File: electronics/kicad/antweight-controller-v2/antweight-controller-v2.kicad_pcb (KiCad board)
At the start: 2 copper layers, 30.5 x 58.4 mm, 11 parts, among them J10 3V3 GND VBAT_SW, J4 BATTERY, J5 MOTOR LEFT, J6 MOTOR RIGHT, J8 ESP32 LEFT ALL PINS, J9 ESP32 RIGHT SIGNALS, SW1 MAIN POWER, U1 ESP32-C3 SUPERMINI, U2 DRV8833, U3 3V3 BUCK-BOOST

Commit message: feat(electronics): finalize v2 controller layout
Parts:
- moved U2 14.7 mm to (22.0, 27.7), turned to 270 degrees
- moved C1_C2 5.08 mm to (18.0, 46.6)
- moved J10 5.08 mm to (12.7, 57.1)
- moved J4 5.08 mm to (18.0, 51.6)
- moved J5 5.08 mm to (4.50, 57.1)
- moved J6 5.08 mm to (25.9, 57.1)
- moved SW1 5.08 mm to (10.2, 51.6)
- moved U3 5.08 mm to (10.2, 46.6)
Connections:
- J9 pad 1: GPIO5_SPARE -> GPIO21_SPARE
- J9 pad 2: AIN2_GPIO6 -> GPIO20_SPARE
- J9 pad 3: AIN1_GPIO7 -> BIN2_GPIO10
- J9 pad 4: GPIO8_LED_EXPANSION -> BIN1_GPIO9
- J9 pad 5: BIN1_GPIO9 -> GPIO8_LED_EXPANSION
- J9 pad 6: BIN2_GPIO10 -> AIN1_GPIO7
- J9 pad 7: GPIO20_SPARE -> AIN2_GPIO6
- J9 pad 8: GPIO21_SPARE -> GPIO5_SPARE
- U1 pad 10: AIN2_GPIO6 -> GPIO20_SPARE
- U1 pad 11: AIN1_GPIO7 -> BIN2_GPIO10
- U1 pad 12: GPIO8_LED_EXPANSION -> BIN1_GPIO9
- U1 pad 13: BIN1_GPIO9 -> GPIO8_LED_EXPANSION
- U1 pad 14: BIN2_GPIO10 -> AIN1_GPIO7
- U1 pad 15: GPIO20_SPARE -> AIN2_GPIO6
- U1 pad 16: GPIO21_SPARE -> GPIO5_SPARE
- U1 pad 9: GPIO5_SPARE -> GPIO21_SPARE
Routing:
- net VBAT_RAW: track 0.00 -> 12.8 mm
- net GPIO4_SPARE: track 0.00 -> 2.54 mm
- net GPIO3_SPARE: track 0.00 -> 2.54 mm
- net GPIO2_SPARE: track 0.00 -> 2.54 mm
- net GPIO1_SPARE: track 0.00 -> 2.54 mm
- net GPIO0_SPARE: track 0.00 -> 2.54 mm
- net GND: track 0.00 -> 2.54 mm
- net 5V_NC: track 0.00 -> 2.54 mm
- net 3V3: track 0.00 -> 2.54 mm
- net GPIO8_LED_EXPANSION: track 0.00 -> 2.54 mm
- net GPIO5_SPARE: track 0.00 -> 2.54 mm
- net GPIO21_SPARE: track 0.00 -> 2.54 mm
- net GPIO20_SPARE: track 0.00 -> 2.54 mm
- net BIN2_GPIO10: track 0.00 -> 2.54 mm
- net BIN1_GPIO9: track 0.00 -> 2.54 mm
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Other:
- board size 30.5 x 58.4 mm -> 30.5 x 63.5 mm
- board text removed: "IN"

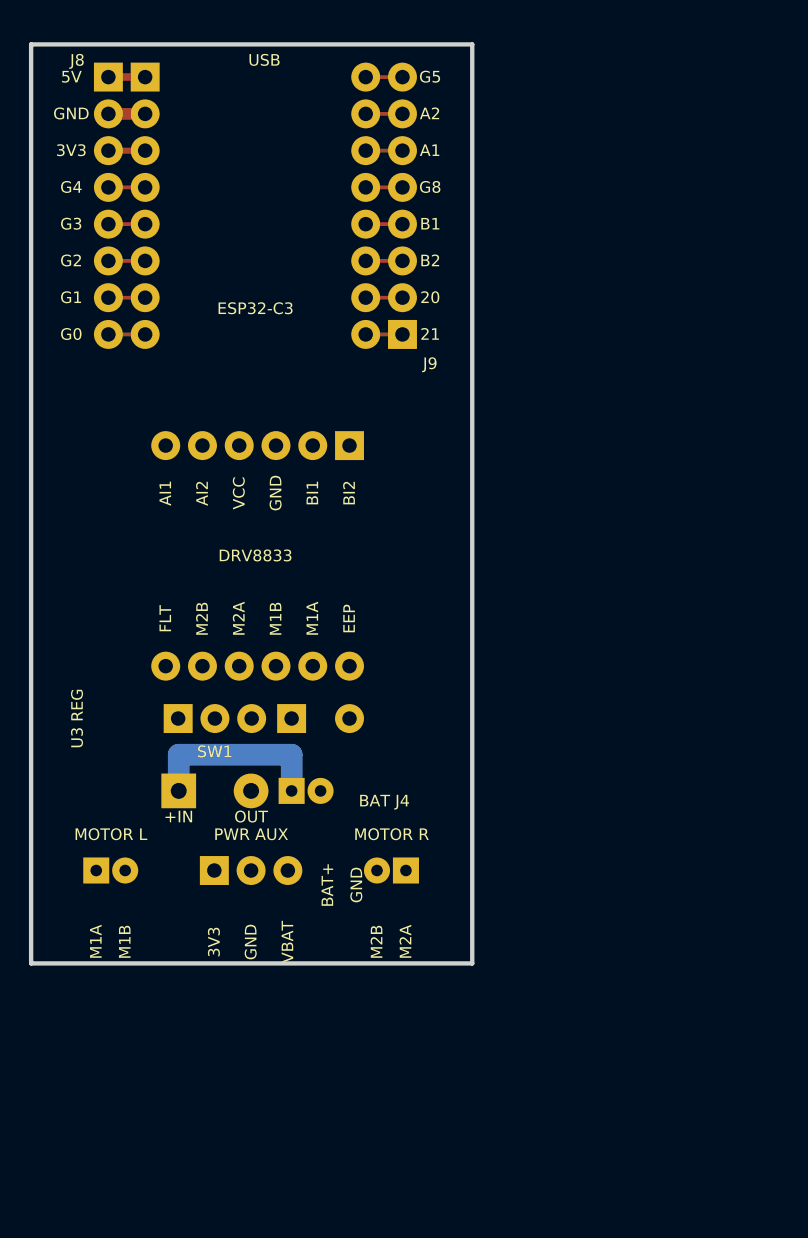
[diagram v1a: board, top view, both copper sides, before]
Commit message: Add 2S antweight controller design
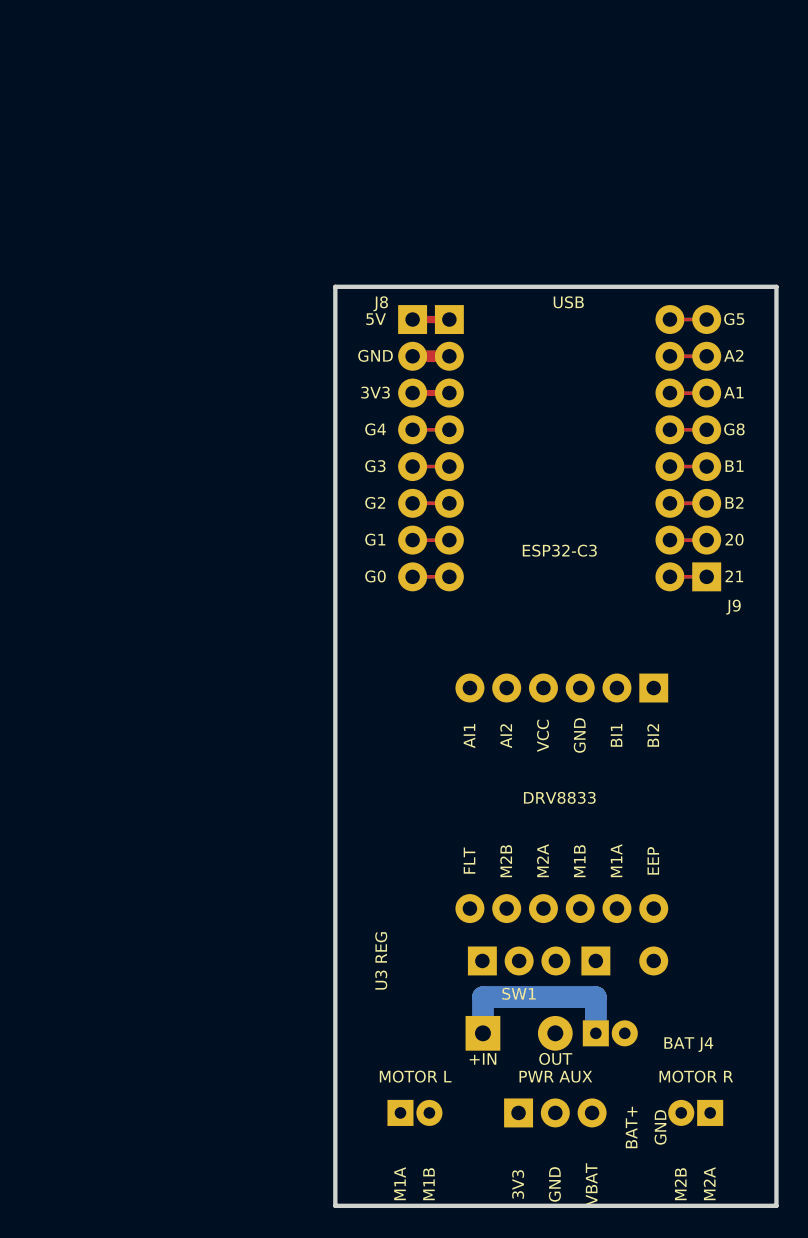
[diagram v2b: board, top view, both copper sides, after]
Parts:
- moved C1_C2 26.9 mm to (39.0, 63.3)
- moved J10 26.9 mm to (33.7, 73.8)
- moved J4 26.9 mm to (39.0, 68.3)
- moved J5 26.9 mm to (25.5, 73.8)
- moved J6 26.9 mm to (46.9, 73.8)
- moved J8 26.9 mm to (26.4, 19.0)
- moved J9 26.9 mm to (46.7, 19.0)
- moved SW1 26.9 mm to (31.2, 68.3)
- moved U1 26.9 mm to (28.9, 19.0)
- moved U2 26.9 mm to (43.0, 44.5)
- moved U3 26.9 mm to (31.2, 63.3)
